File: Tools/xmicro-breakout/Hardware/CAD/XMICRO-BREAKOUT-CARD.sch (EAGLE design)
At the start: 3 parts, among them J1 HDR-17X2, J2 HDR-17X2, P1 XMICRO-BUS-PHYSICAL-EDGE62M

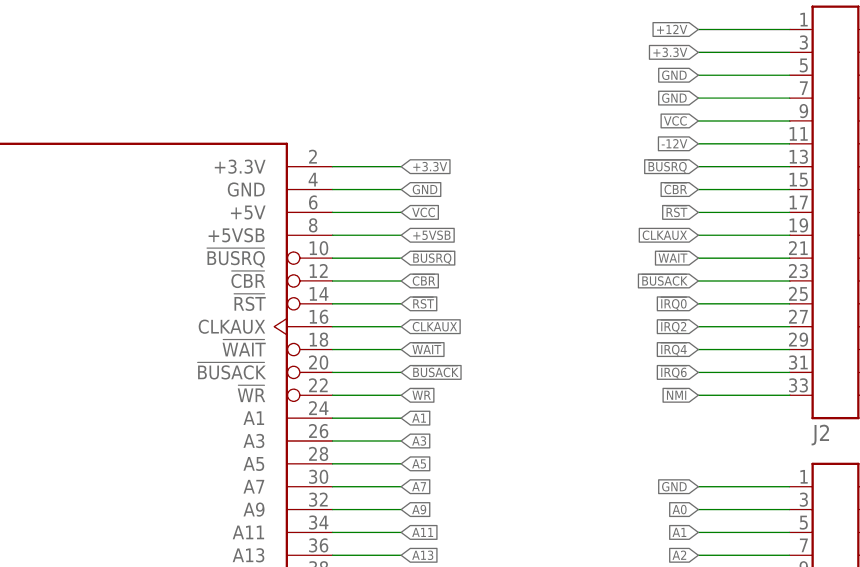
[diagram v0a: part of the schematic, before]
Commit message: Fixed tools with new IOSEL signal
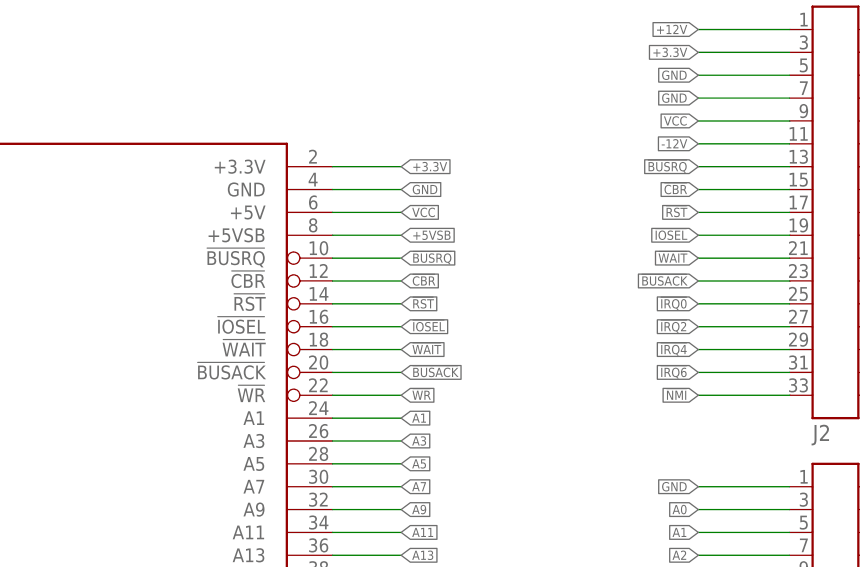
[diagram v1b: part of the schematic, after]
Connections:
- removed net CLKAUX: J1.19, P1.CLKAUX@16
- new net !IOSEL: J1.19, P1.!IOSEL@16
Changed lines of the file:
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@@
 </segment>
 </net>
-<net name="CLKAUX" class="0">
+<net name="!IOSEL" class="0">
 <segment>
 <wire x1="124.46" y1="121.92" x2="132.08" y2="121.92" width="0.1524" layer="91"/>
 <label x="132.08" y="121.92" size="1.016" layer="95" xref="yes"/>
-<pinref part="P1" gate="G$1" pin="CLKAUX@16"/>
+<pinref part="P1" gate="G$1" pin="!IOSEL@16"/>
 </segment>
 <segment>
